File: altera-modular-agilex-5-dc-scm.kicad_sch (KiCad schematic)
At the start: 0 parts

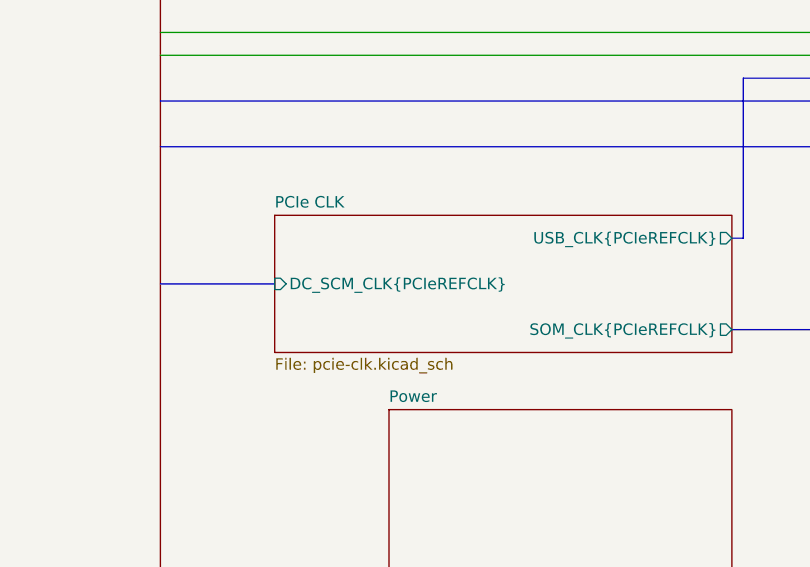
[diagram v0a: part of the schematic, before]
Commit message: [#99871] Rename PCIe CLK schematic sheet to CLK
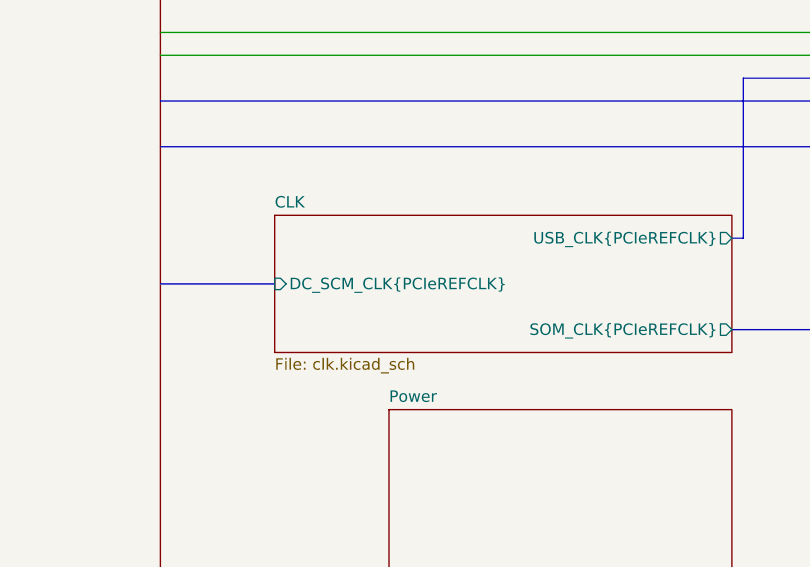
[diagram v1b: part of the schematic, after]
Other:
- sheet PCIe CLK renamed CLK
- sheet CLK: file pcie-clk.kicad_sch -> clk.kicad_sch
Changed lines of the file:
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@@
 			(color 0 0 0 0)
 		)
-		(property "Sheetname" "PCIe CLK"
+		(property "Sheetname" "CLK"
 			(at 88.9 60.2484 0)
 			(show_name no)
@@
 			)
 		)
-		(property "Sheetfile" "pcie-clk.kicad_sch"
+		(property "Sheetfile" "clk.kicad_sch"
 			(at 88.9 76.7846 0)
 			(show_name no)

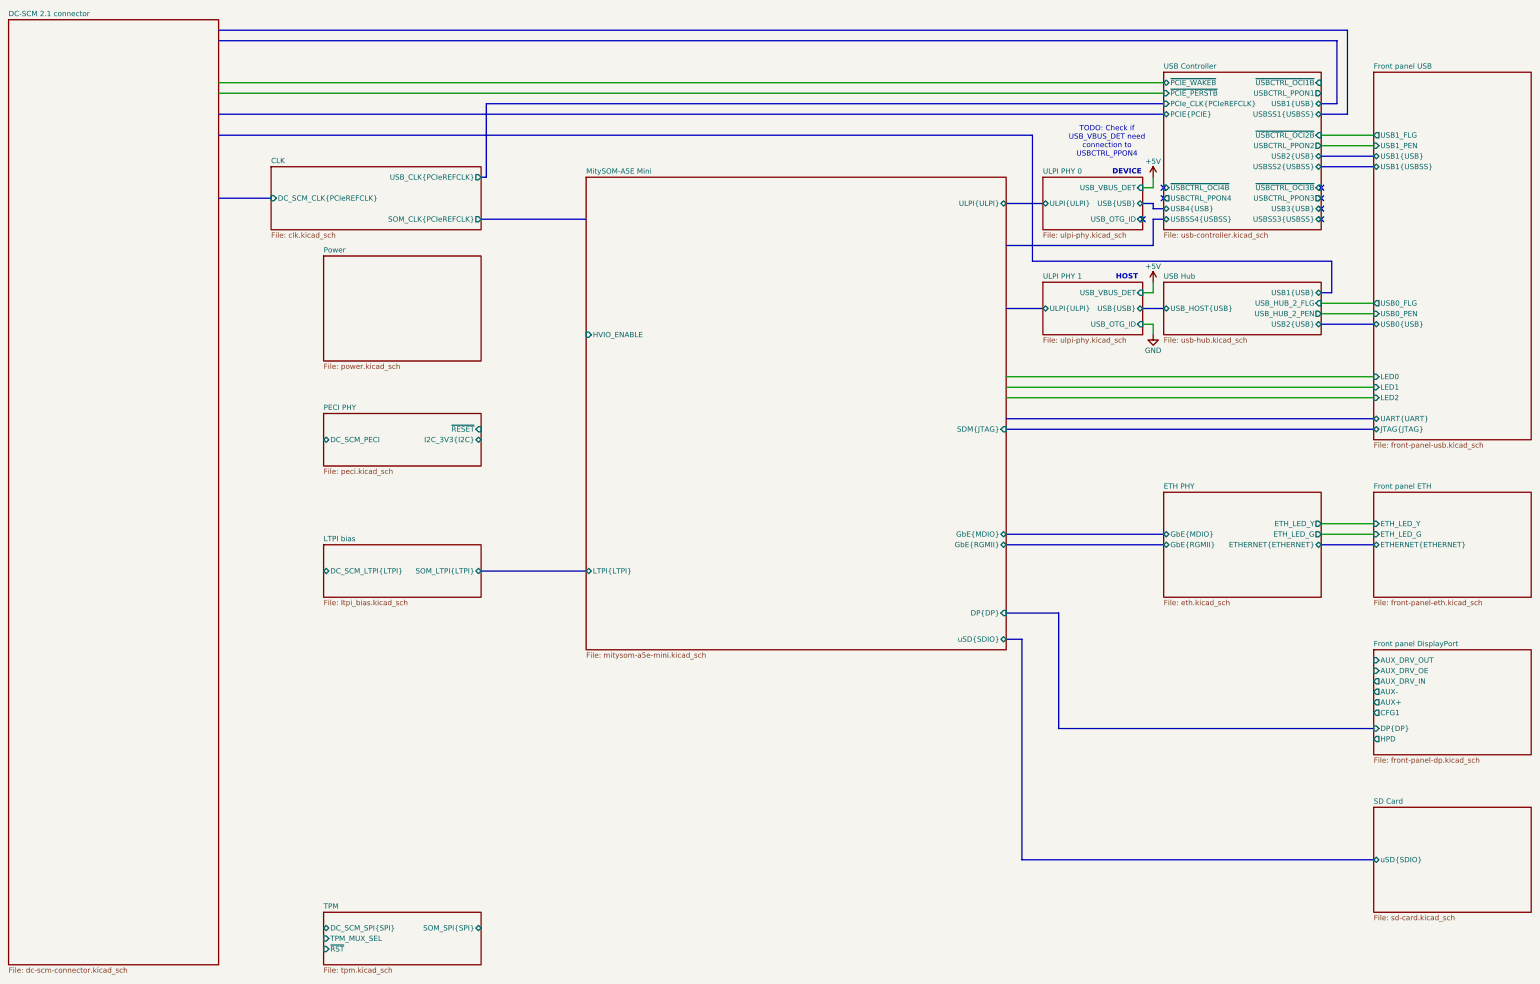
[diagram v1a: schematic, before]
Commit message: [#99871] Import ports from CLK sheet to root schematic
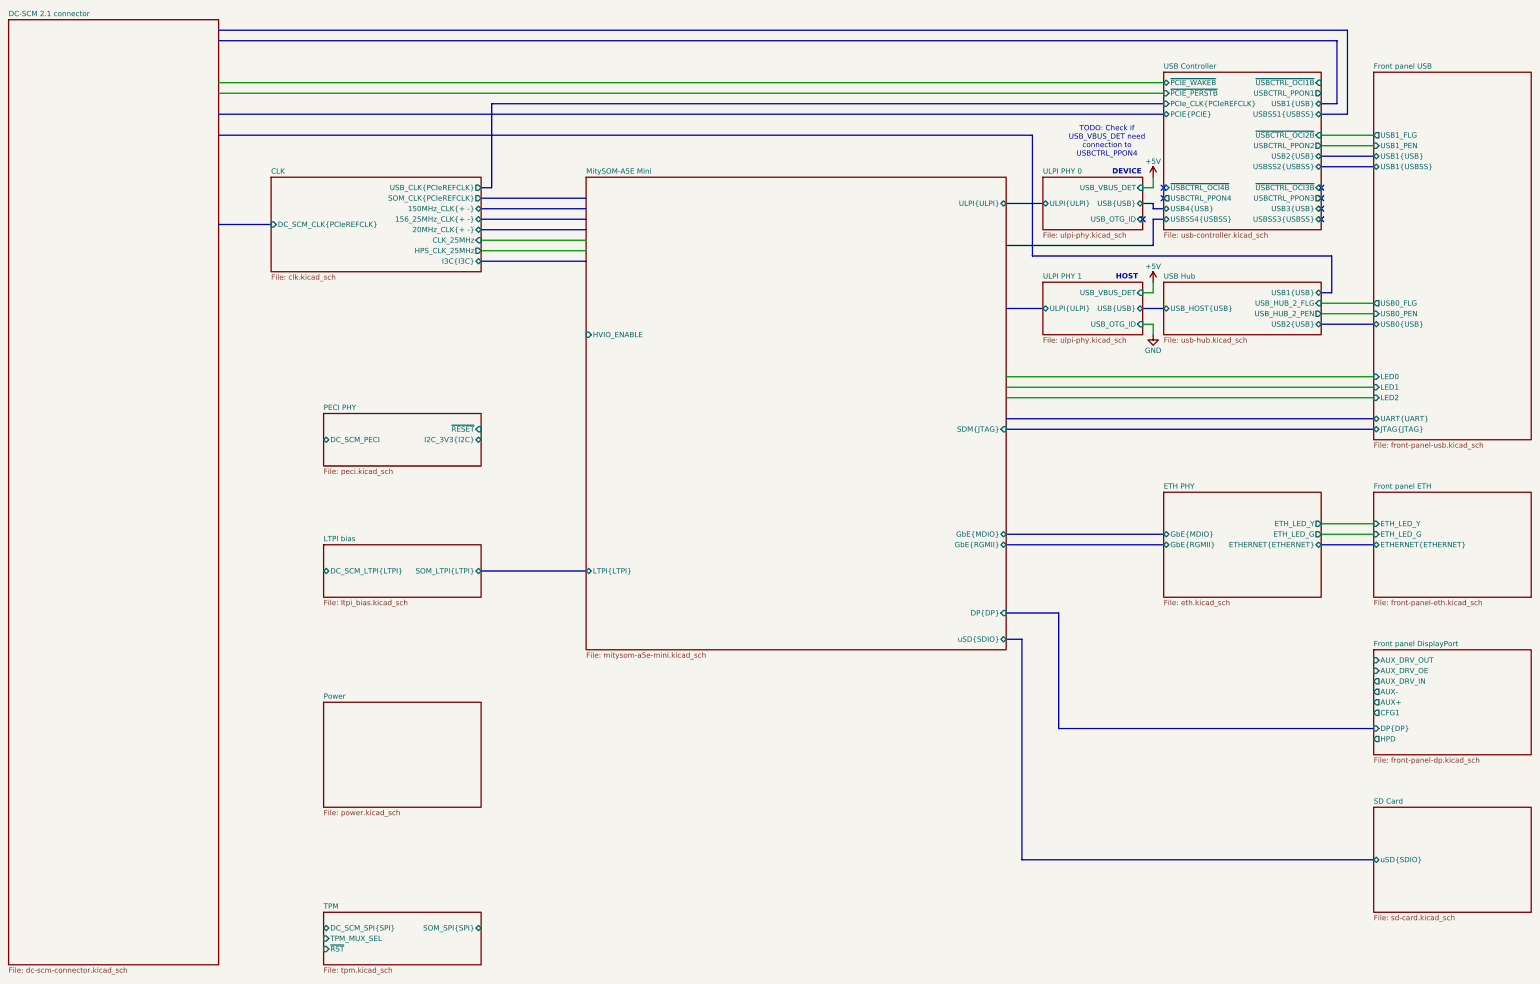
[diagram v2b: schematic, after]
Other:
- sheet CLK ports: added 150MHz_CLK{+ -}, 156_25MHz_CLK{+ -}, 20MHz_CLK{+ -}, CLK_25MHz, HPS_CLK_25MHz, I3C{I3C}; removed none

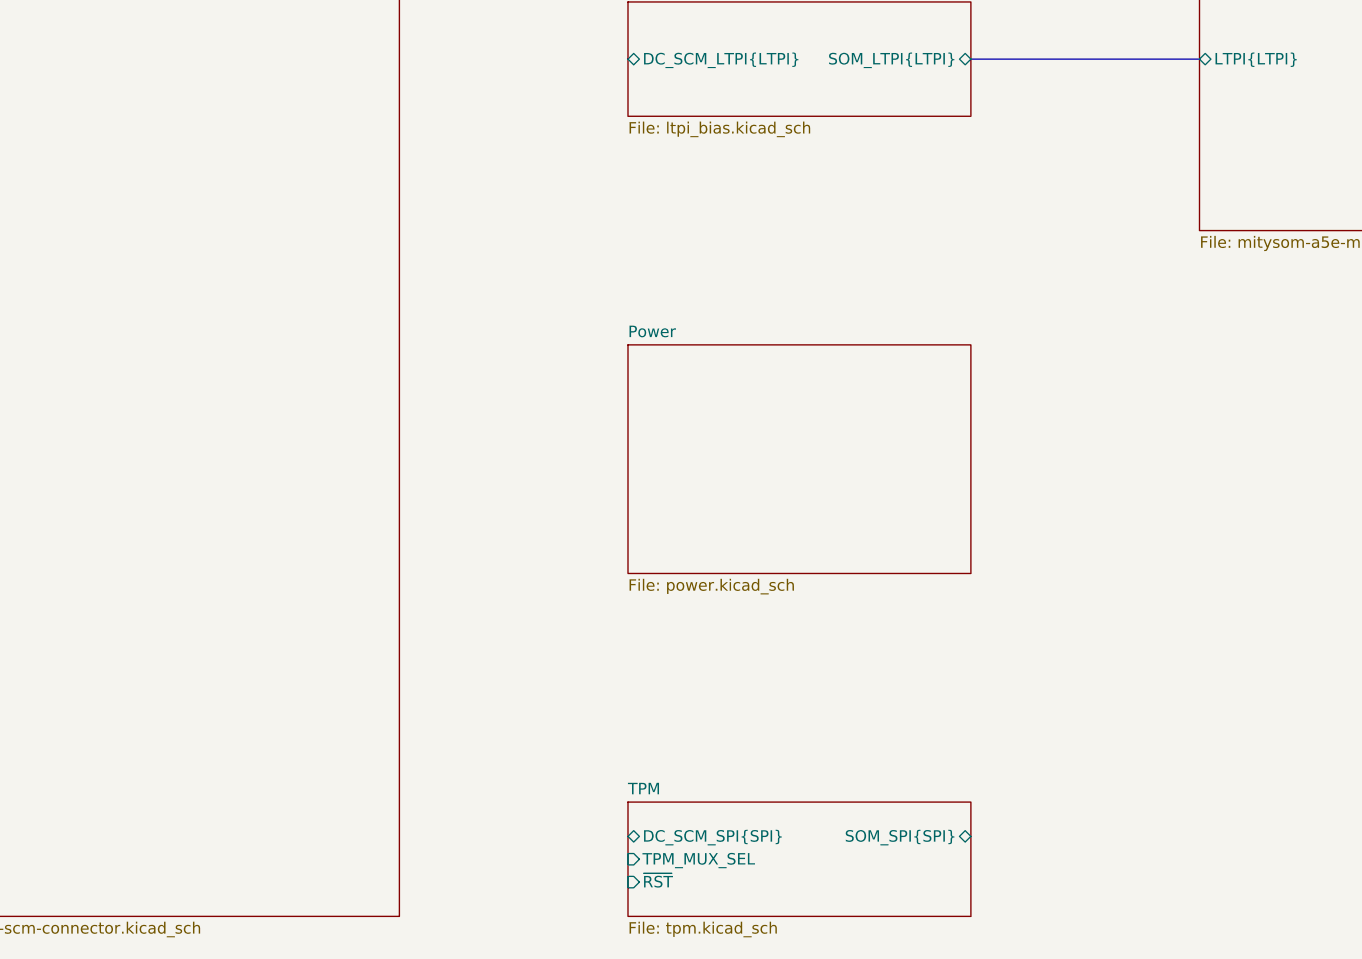
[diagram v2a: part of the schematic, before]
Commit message: [#99732] Fix TMP connection - connect via MUX to SPI and QSPI from DC-SCM
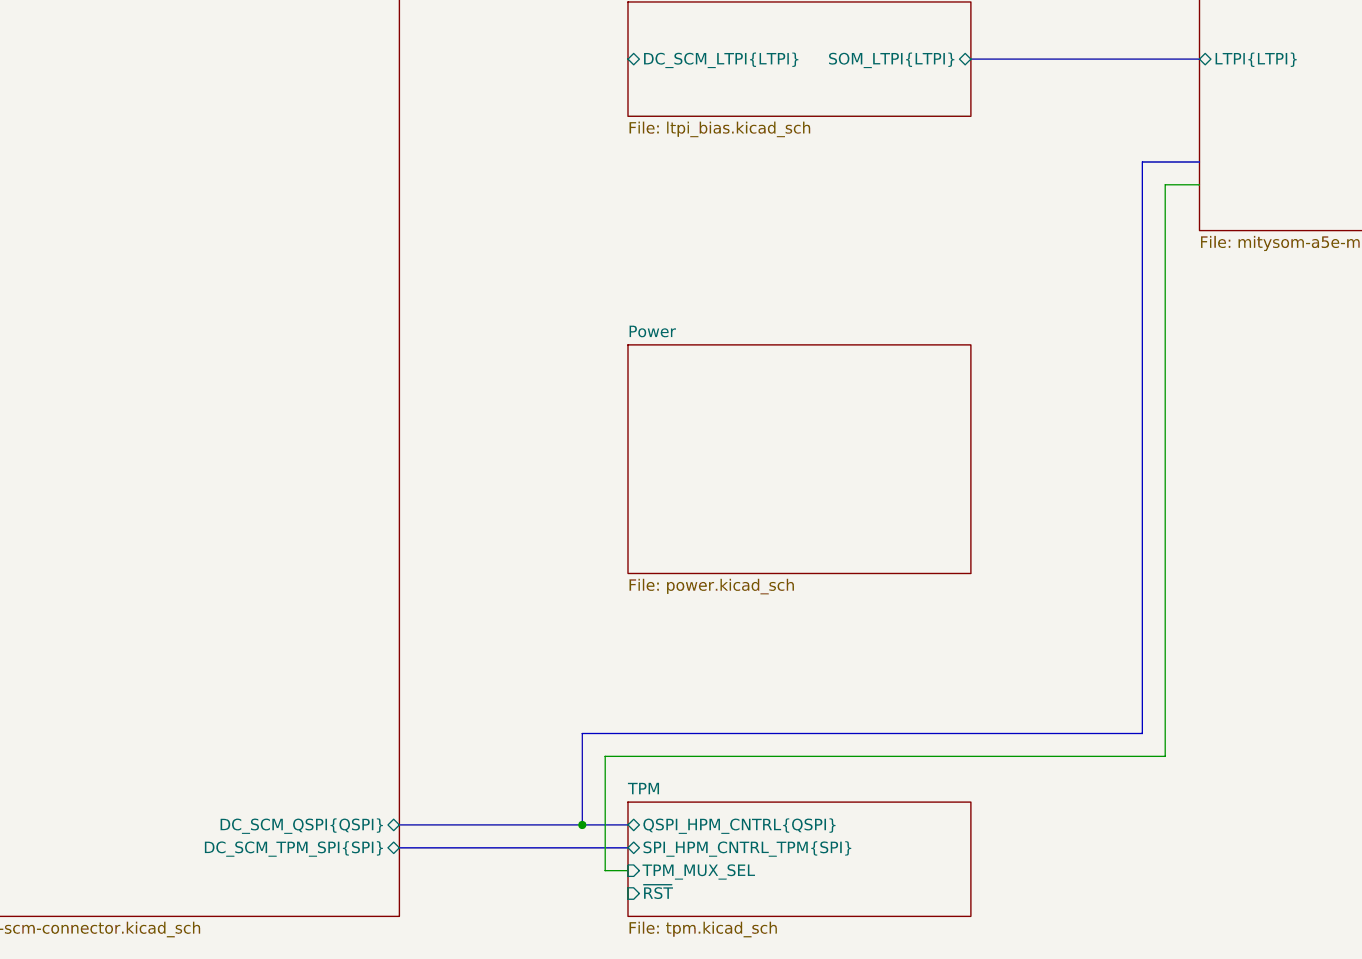
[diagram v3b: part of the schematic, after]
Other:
- sheet DC-SCM 2.1 connector ports: added DC_SCM_QSPI{QSPI}, DC_SCM_TPM_SPI{SPI}; removed none
- sheet TPM ports: added QSPI_HPM_CNTRL{QSPI}, SPI_HPM_CNTRL_TPM{SPI}; removed DC_SCM_SPI{SPI}, SOM_SPI{SPI}
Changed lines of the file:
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@@
 		)
+	)
+	(junction
+		(at 96.52 243.84)
+		(diameter 0)
+		(color 0 0 0 0)
 	)
 	(no_connect
@@
 		)
 	)
+	(bus
+		(pts
+			(xy 158.75 170.18) (xy 158.75 233.68)
+		)
+		(stroke
+			(width 0)
+			(type default)
+		)
+	)
 	(wire
 		(pts
@@
 	(wire
 		(pts
+			(xy 161.29 172.72) (xy 165.1 172.72)
+		)
+		(stroke
+			(width 0)
+			(type default)
+		)
+	)
+	(wire
+		(pts
 			(xy 302.26 91.44) (xy 299.72 91.44)
 		)
@@
 	(bus
 		(pts
+			(xy 76.2 246.38) (xy 101.6 246.38)
+		)
+		(stroke
+			(width 0)
+			(type default)
+		)
+	)
+	(bus
+		(pts
+			(xy 76.2 243.84) (xy 96.52 243.84)
+		)
+		(stroke
+			(width 0)
+			(type default)
+		)
+	)
+	(wire
+		(pts
+			(xy 161.29 172.72) (xy 161.29 236.22)
+		)
+		(stroke
+			(width 0)
+			(type default)
+		)
+	)
+	(bus
+		(pts
 			(xy 139.7 68.58) (xy 165.1 68.58)
 		)
@@
 	(bus
 		(pts
+			(xy 96.52 233.68) (xy 96.52 243.84)
+		)
+		(stroke
+			(width 0)
+			(type default)
+		)
+	)
+	(bus
+		(pts
 			(xy 342.9 91.44) (xy 345.44 91.44)
 		)
@@
 		)
 	)
+	(bus
+		(pts
+			(xy 96.52 233.68) (xy 158.75 233.68)
+		)
+		(stroke
+			(width 0)
+			(type default)
+		)
+	)
 	(wire
 		(pts
@@
 		)
 	)
+	(wire
+		(pts
+			(xy 101.6 248.92) (xy 99.06 248.92)
+		)
+		(stroke
+			(width 0)
+			(type default)
+		)
+	)
 	(bus
 		(pts
@@
 	(wire
 		(pts
+			(xy 99.06 236.22) (xy 99.06 248.92)
+		)
+		(stroke
+			(width 0)
+			(type default)
+		)
+	)
+	(wire
+		(pts
 			(xy 266.7 114.3) (xy 355.6 114.3)
 		)
@@
 	(bus
 		(pts
+			(xy 158.75 170.18) (xy 165.1 170.18)
+		)
+		(stroke
+			(width 0)
+			(type default)
+		)
+	)
+	(bus
+		(pts
+			(xy 96.52 243.84) (xy 101.6 243.84)
+		)
+		(stroke
+			(width 0)
+			(type default)
+		)
+	)
+	(bus
+		(pts
 			(xy 266.7 152.4) (xy 304.8 152.4)
+		)
+		(stroke
+			(width 0)
+			(type default)
+		)
+	)
+	(wire
+		(pts
+			(xy 99.06 236.22) (xy 161.29 236.22)
 		)
 		(stroke
@@
 			)
 		)
+		(pin "DC_SCM_QSPI{QSPI}" bidirectional
+			(at 76.2 243.84 0)
+			(effects
+				(font
+					(size 1.27 1.27)
+				)
+				(justify right)
+			)
+		)
+		(pin "DC_SCM_TPM_SPI{SPI}" bidirectional
+			(at 76.2 246.38 0)
+			(effects
+				(font
+					(size 1.27 1.27)
+				)
+				(justify right)
+			)
+		)
 		(instances
 			(project "altera-modular-agilex-5-dc-scm"
@@
 		)
 		(pin "TPM_MUX_SEL" input
-			(at 101.6 247.65 180)
+			(at 101.6 248.92 180)
 			(effects
 				(font
@@
 		)
 		(pin "~{RST}" input
-			(at 101.6 250.19 180)
-			(effects
-				(font
-					(size 1.27 1.27)
-				)
-				(justify left)
-			)
-		)
-		(pin "SOM_SPI{SPI}" bidirectional
-			(at 139.7 245.11 0)
-			(effects
-				(font
-					(size 1.27 1.27)
-				)
-				(justify right)
-			)
-		)
-		(pin "DC_SCM_SPI{SPI}" bidirectional
-			(at 101.6 245.11 180)
-			(effects
-				(font
+			(at 101.6 251.46 180)
+			(effects
+				(font
+					(size 1.27 1.27)
+				)
+				(justify left)
+			)
+		)
+		(pin "QSPI_HPM_CNTRL{QSPI}" bidirectional
+			(at 101.6 243.84 180)
+			(effects
+				(font
+					(size 1.27 1.27)
+				)
+				(justify left)
+			)
+		)
+		(pin "SPI_HPM_CNTRL_TPM{SPI}" bidirectional
+			(at 101.6 246.38 180)
+			(effects
+				(font
